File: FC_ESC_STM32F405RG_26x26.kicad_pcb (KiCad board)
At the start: 2 copper layers, 37 x 34 mm, 231 parts, among them J1 Conn_01x02, J10 Conn_01x01, J11 Conn_01x02, J12 Conn_02x02_Odd_Even, J13 ALARM, J14 LED_STRIP, J16 MOTOR, J17 MOTOR, J18 MOTOR, J19 MOTOR, J2 Conn_02x04_Odd_Even, J20 USB_A, J21 ESC_PROG, J23 ESC_PROG, J24 ESC_PROG, J25 ESC_PROG, J3 Debugger, J4 Conn_01x04, J5 RSSI, J6 Conn_01x04, J7 Conn_01x02, J8 Conn_01x04, J9 LED_STRIP, Q1 SIZ200, Q10 SIZ200, Q11 SIZ200, Q12 SIZ200, Q2 SIZ200, Q3 SIZ200, Q4 SIZ200, Q5 SIZ200, Q6 SIZ200, Q7 SIZ200, Q8 SIZ200, Q9 SIZ200, U1 EFM8BB21, U10 FD6288Q, U11 outline, U12 MPU-6000, U13 BMP280, U15 STM32F405RGTx, U16 TPS54331D, U2 EFM8BB21, U3 TPS54560BDDA, U4 FD6288Q, U5 FD6288Q, U6 AT7456, U7 EFM8BB21, U8 EFM8BB21, U9 FD6288Q, Y1 8MHz, Y2 8Mhz

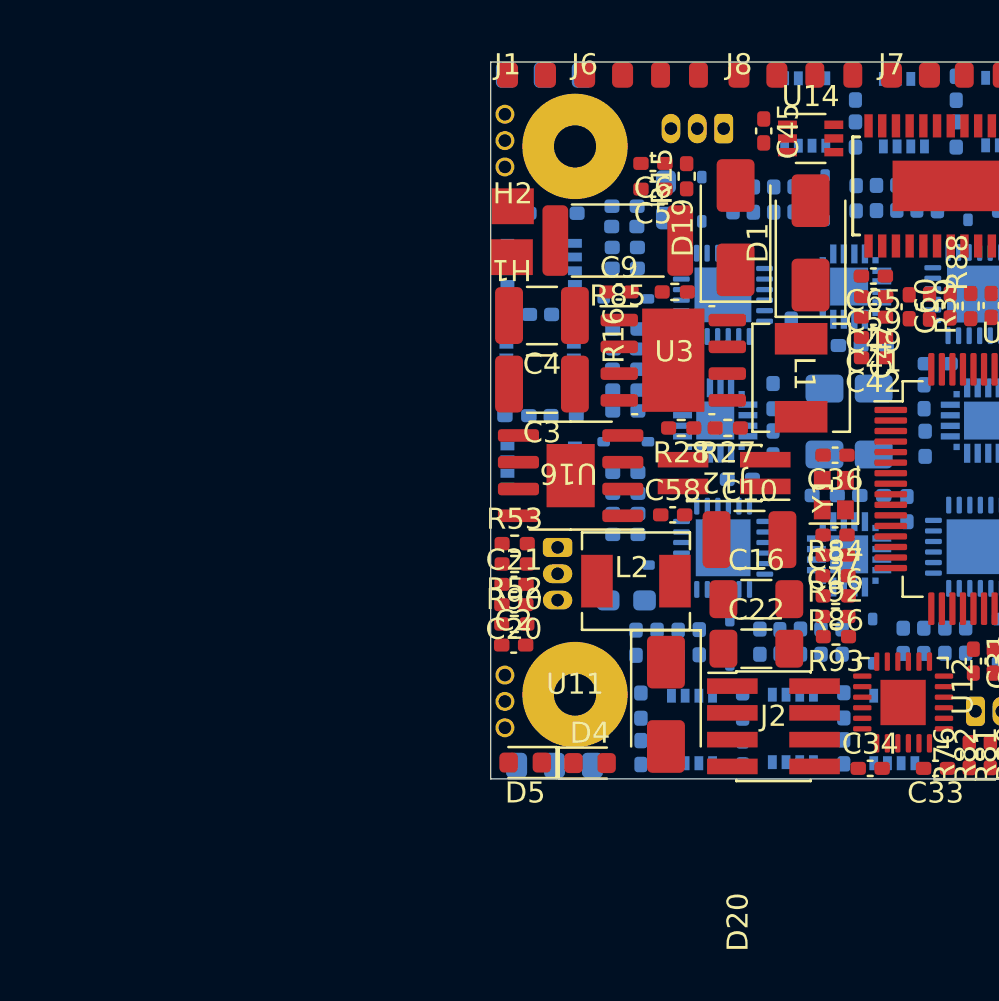
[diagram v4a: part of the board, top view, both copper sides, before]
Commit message: update placement
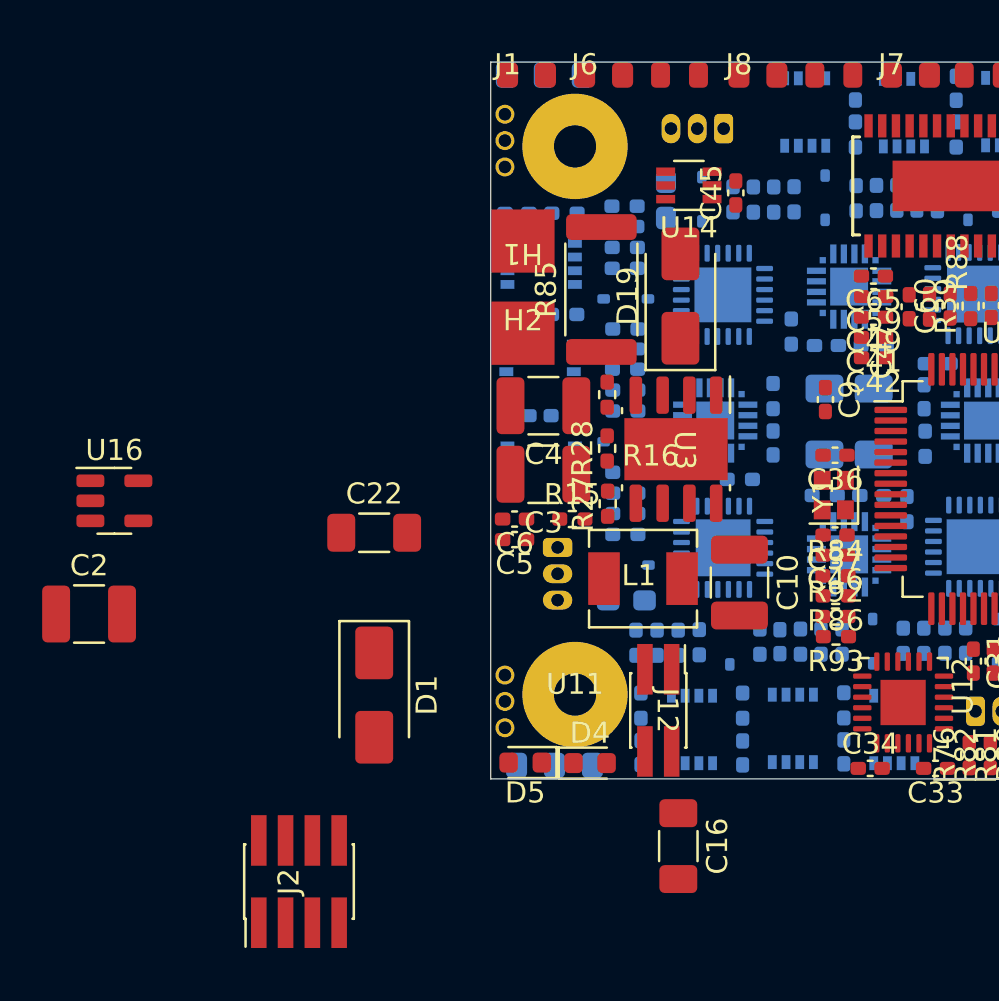
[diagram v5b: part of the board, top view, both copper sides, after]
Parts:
- removed C20: 10pF, Capacitor_SMD:C_0402_1005Metric_Pad0.74x0.62mm_HandSolder
- removed C21: 100nF, Capacitor_SMD:C_0402_1005Metric_Pad0.74x0.62mm_HandSolder
- removed C58: 8.2nF, Capacitor_SMD:C_0402_1005Metric_Pad0.74x0.62mm_HandSolder
- removed D20: SS34, Diode_SMD:D_SMA
- removed L2: 4uH, Proj_footprint:Inductor
- removed R52: 10k2, Resistor_SMD:R_0402_1005Metric_Pad0.72x0.64mm_HandSolder
- removed R53: 3.24k, Resistor_SMD:R_0402_1005Metric_Pad0.72x0.64mm_HandSolder
- removed R90: 28.7k, Resistor_SMD:R_0402_1005Metric_Pad0.72x0.64mm_HandSolder
- C2: value 1nF -> 100uF; footprint Capacitor_SMD:C_0402_1005Metric_Pad0.74x0.62mm_HandSolder -> Capacitor_SMD:C_1210_3225Metric_Pad1.33x2.70mm_HandSolder
- U16: value TPS54331D -> RT9013-33GB; footprint Proj_footprint:SOIC-8-1EP_3.9x4.9mm_P1.27mm_EP2.29x3mm -> Package_TO_SOT_SMD:SOT-23-5
- moved D1 29.8 mm to (193.0, 93.3), turned to -90 degrees
- moved J2 23.7 mm to (189.5, 102.1), turned to 90 degrees
- moved U16 21.6 mm to (180.7, 84.0), turned to 0 degrees
- moved C2 20.2 mm to (179.5, 89.4)
- moved C22 18.9 mm to (193.0, 85.6)
- moved C6 18.1 mm to (199.7, 84.9)
- moved C5 17.9 mm to (199.7, 85.9)
- moved R15 17.1 mm to (202.4, 84.9), turned to 0 degrees
- moved C16 12.3 mm to (207.5, 100.4), turned to -90 degrees
- moved L1 12.1 mm to (205.8, 87.7), turned to 0 degrees
- moved J12 11.8 mm to (206.4, 94.0), turned to -90 degrees
- moved C9 11.0 mm to (214.4, 79.2), turned to -90 degrees
- moved R27 6.74 mm to (204.1, 84.2), turned to 90 degrees
- moved U14 6.19 mm to (208.0, 69.1), turned to 180 degrees
- moved H2 6.04 mm to (200.1, 76.1)
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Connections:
- C2 pad 1: Net-(C2-Pad1) -> Net-(J2-Pin_3)
- U16 pad 1: Net-(U16-BOOT) -> +5V
- U16 pad 2: +5V -> GND
- U16 pad 4: Net-(U16-SS) -> (no net)
- U16 pad 5: Net-(U16-VSENSE) -> Net-(J2-Pin_3)

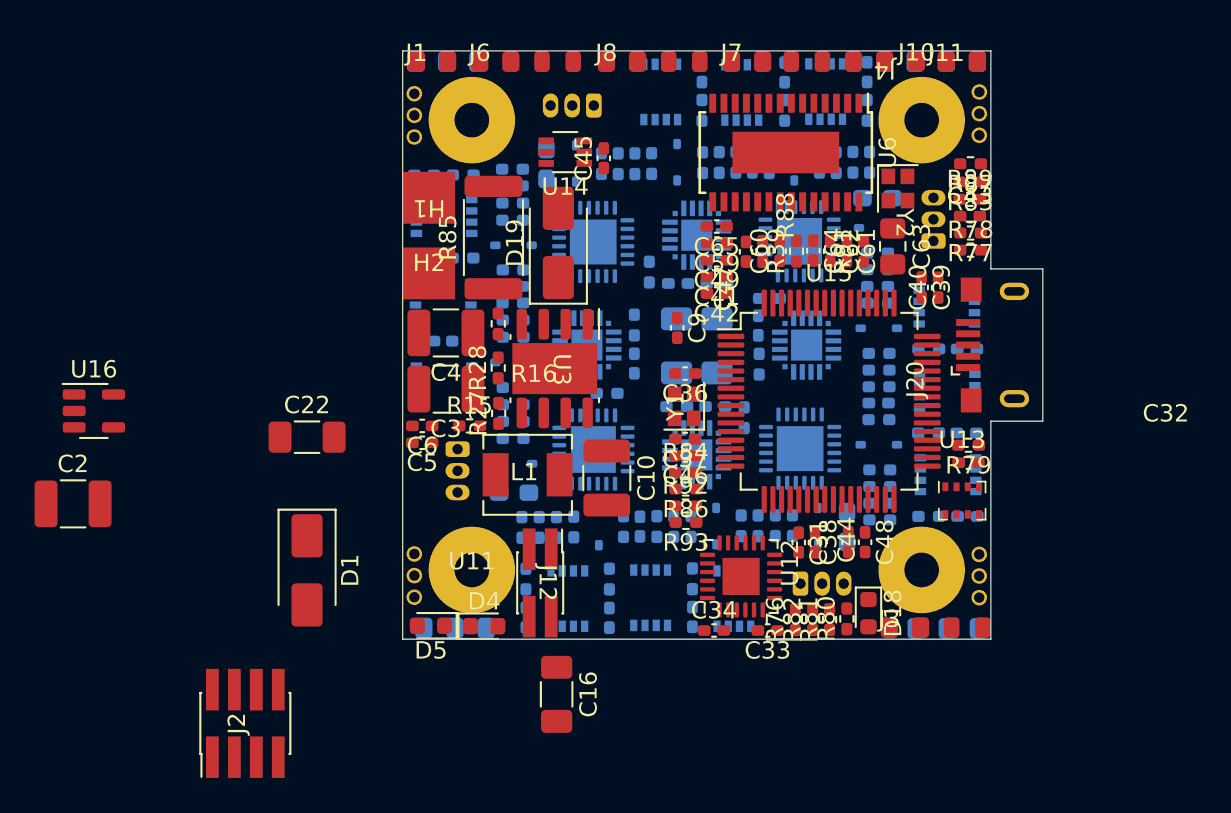
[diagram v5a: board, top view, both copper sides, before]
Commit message: update placement
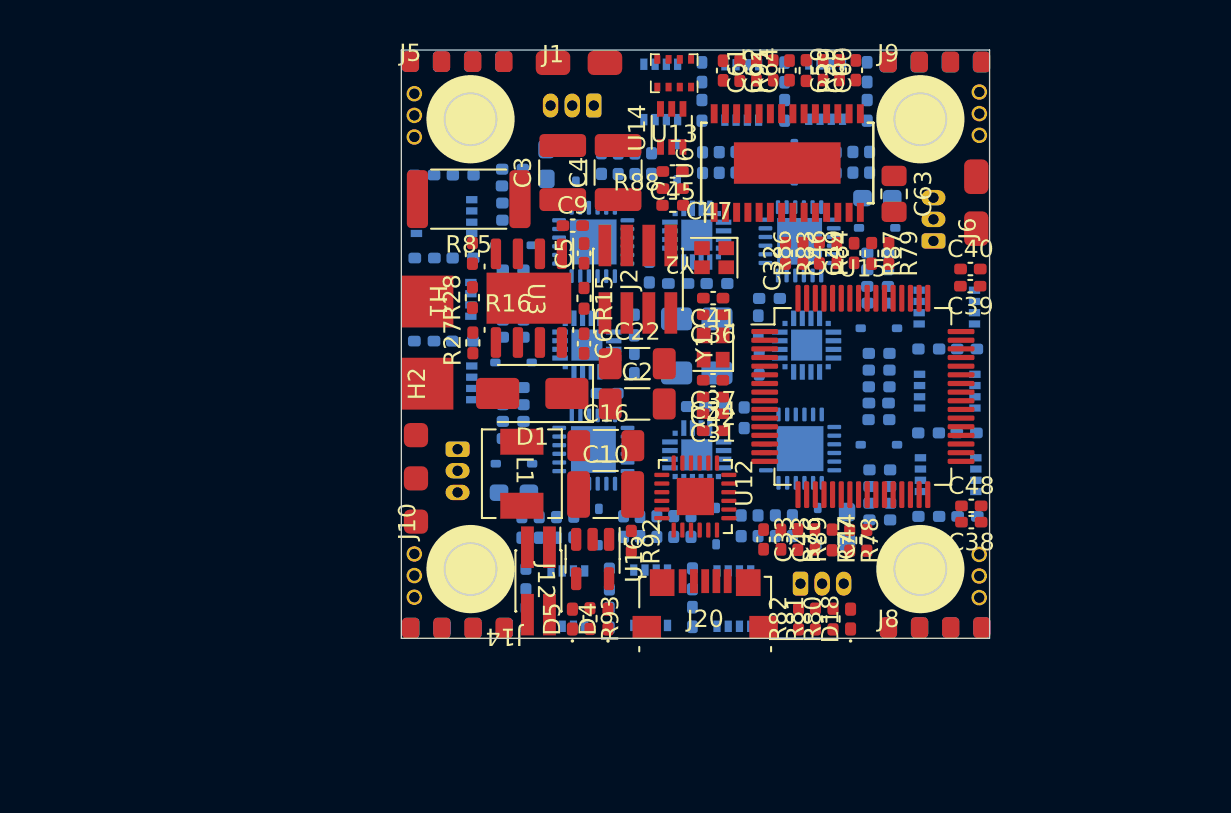
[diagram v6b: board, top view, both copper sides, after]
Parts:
- removed D19: SS34, Diode_SMD:D_SMA
- removed J11: Conn_01x02, Proj_footprint:MountingPad_1x2
- removed J13: ALARM, Proj_footprint:MountingPad_1x3
- removed J7: Conn_01x02, Proj_footprint:MountingPad_5VOUT
- added J15: Conn_01x04, Proj_footprint:MountingPad_1x4, B.Cu at (226.6, 96.6)
- added J26: Conn_01x04, Proj_footprint:MountingPad_1x4, B.Cu at (204.4, 63.8)
- C2: footprint Capacitor_SMD:C_1210_3225Metric_Pad1.33x2.70mm_HandSolder -> Capacitor_SMD:C_1206_3216Metric_Pad1.33x1.80mm_HandSolder
- D18, D4, D5: footprint LED_SMD:LED_0603_1608Metric -> LED_SMD:LED_0402_1005Metric_Pad0.77x0.64mm_HandSolder
- J1: footprint Proj_footprint:MountingPad_5VOUT -> Proj_footprint:MountingPad_1x2
- J10: value Conn_01x01 -> LED_STRIP; footprint Proj_footprint:MountingPad_1x1 -> Proj_footprint:MountingPad_1x3
- J14, J9: value LED_STRIP -> Conn_01x04; footprint Proj_footprint:MountingPad_1x3 -> Proj_footprint:MountingPad_1x4; moved to F.Cu
- J20: footprint Proj_footprint:USB_Micro-B_2P_4hole -> Proj_footprint:USB_Micro-B_SMD
- J3, J4: moved to B.Cu
- J5: value RSSI -> Conn_01x04; footprint Proj_footprint:MountingPad_1x3 -> Proj_footprint:MountingPad_1x4; moved to F.Cu
- J6: value Conn_01x04 -> Conn_01x02; footprint Proj_footprint:MountingPad_1x4 -> Proj_footprint:MountingPad_1x2
- moved J9 40.1 mm to (226.6, 63.9), turned to 0 degrees
- moved J4 39.4 mm to (204.4, 96.6)
- moved J10 39.3 mm to (199.3, 90.4), turned to 90 degrees
- moved J8 36.6 mm to (226.6, 96.6)
- moved J2 34.3 mm to (212.2, 76.4)
- moved C2 33.1 mm to (212.1, 83.6)
- moved J3 32.7 mm to (226.6, 63.9)
- moved J6 30.3 mm to (231.7, 73.5), turned to 90 degrees
- moved U16 30.1 mm to (209.5, 92.6), turned to -90 degrees
- moved U13 29.8 mm to (214.2, 64.5), turned to 180 degrees
- moved J5 29.2 mm to (199.0, 63.8)
- moved C32 26.7 mm to (217.1, 64.4), turned to -90 degrees
- moved J20 25.8 mm to (216.0, 96.6), turned to 0 degrees
- moved J14 23.8 mm to (204.4, 96.6), turned to 180 degrees
- moved R89 22.0 mm to (221.4, 91.5), turned to -90 degrees
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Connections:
- J1 pad 1: GND -> +5V
- J1 pad 2: +5V -> GND
- J10 pad 1: RCIN_INT -> +5V
- J14 pad 2: LED_STRIP -> UART1_RX
- J14 pad 3: GND -> UART1_TX
- J4 pad 1: SENS_RSSI -> +5V
- J4 pad 2: STM32_PA1 -> SENS_RSSI
- J4 pad 3: STM32_PB10 -> STM32_PA1
- J4 pad 4: STM32_PB11 -> GND
- J5 pad 1: +5V -> SPI2_CS
- J5 pad 2: RSSI_IN -> SPI2_MOSI
- J5 pad 3: GND -> SPI2_MISO
- J6 pad 1: SPI2_CS -> +5V
- J6 pad 2: SPI2_MOSI -> GND
- J8 pad 1: UART6_TX -> +5V
- J8 pad 2: UART6_RX -> UART6_TX
- J8 pad 3: UART1_RX -> UART6_RX
- J8 pad 4: UART1_TX -> GND
- J9 pad 2: PWM_OUT -> OSD_VIDEO_OUT
- J9 pad 3: GND -> OSD_VIDEO_IN
- U15 pad 39: PWM_OUT -> unconnected-(U15-PC8-Pad39)
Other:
- board size 37 x 34 mm -> 34 x 34 mm

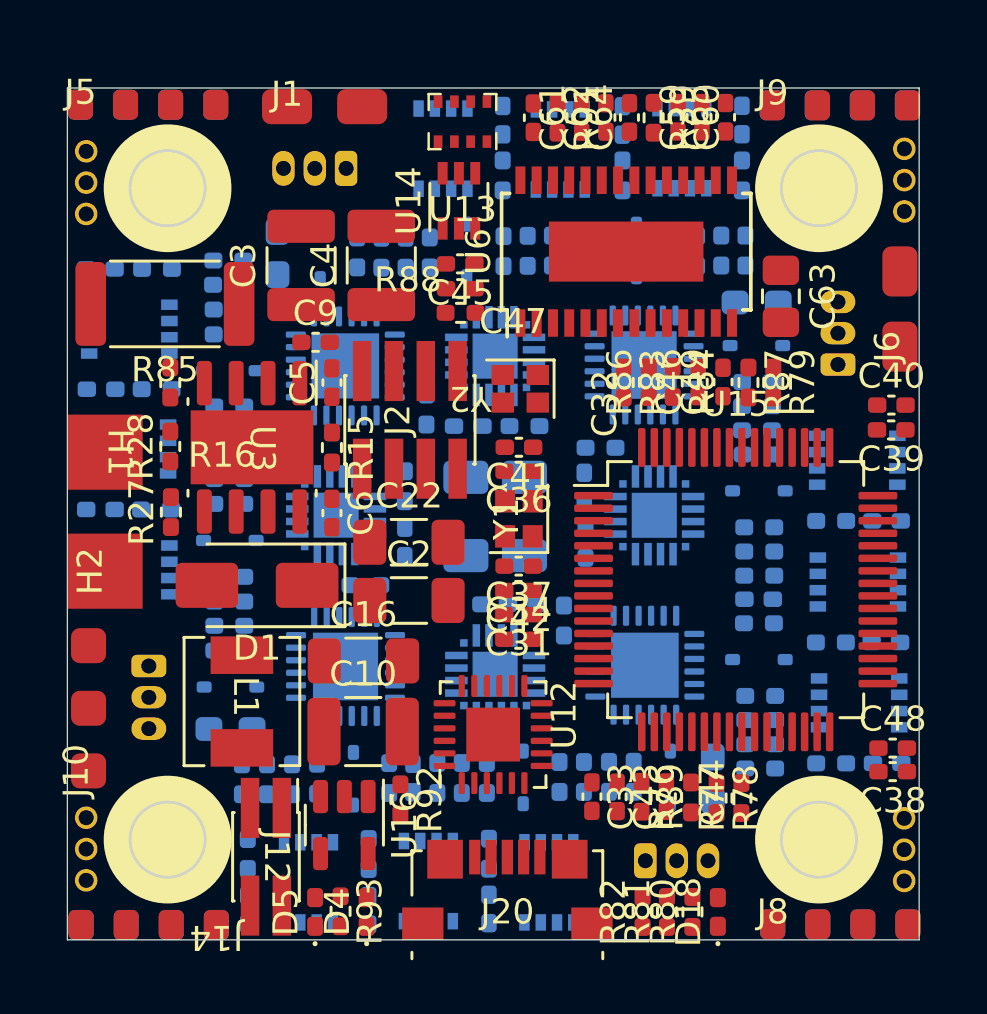
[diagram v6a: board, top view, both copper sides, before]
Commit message: update placement
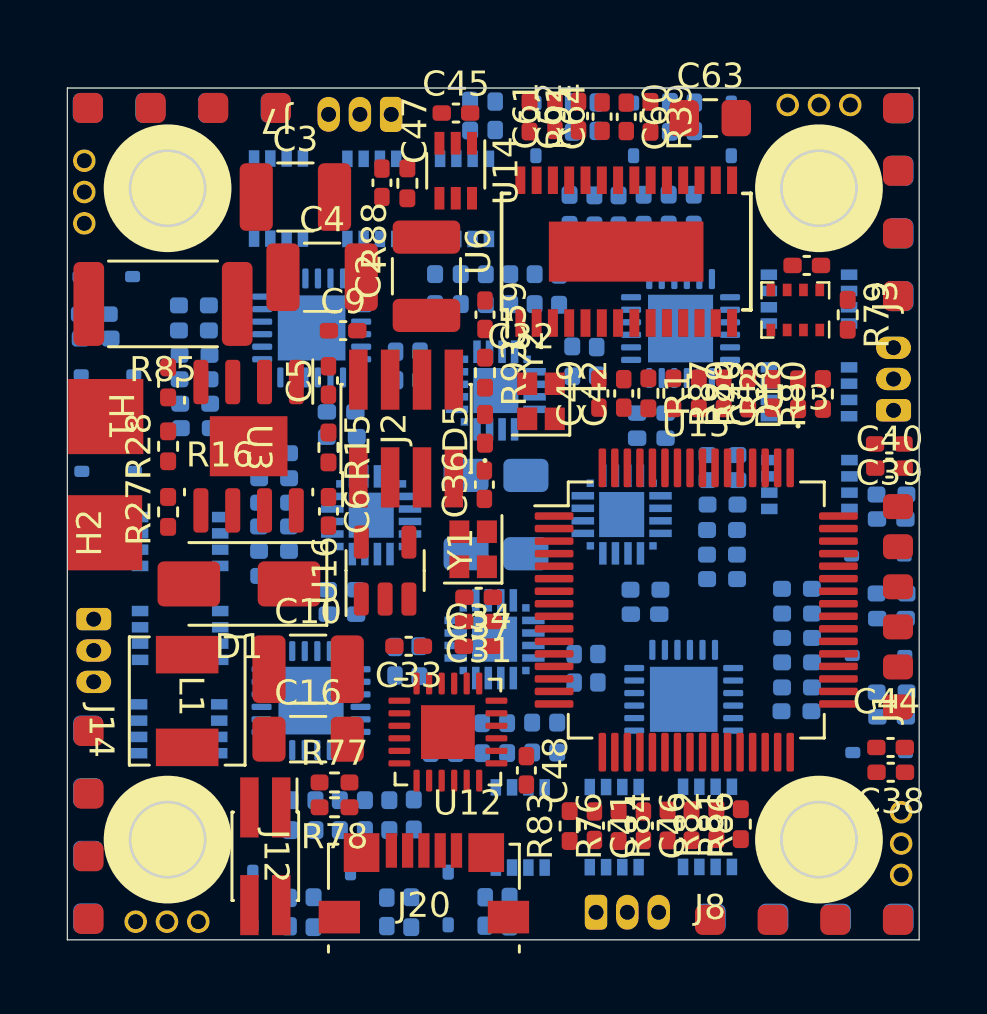
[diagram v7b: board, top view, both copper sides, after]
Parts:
- removed C22: 100uF, Capacitor_SMD:C_1206_3216Metric_Pad1.33x1.80mm_HandSolder
- removed C65: 100nF, Capacitor_SMD:C_0402_1005Metric_Pad0.74x0.62mm_HandSolder
- removed D4: LED_RED, LED_SMD:LED_0402_1005Metric_Pad0.77x0.64mm_HandSolder
- removed J10: LED_STRIP, Proj_footprint:MountingPad_1x3
- removed J5: Conn_01x04, Proj_footprint:MountingPad_1x4
- removed J6: Conn_01x02, Proj_footprint:MountingPad_1x2
- removed R41: 1k, Resistor_SMD:R_0402_1005Metric_Pad0.72x0.64mm_HandSolder
- removed R92: 100R, Resistor_SMD:R_0402_1005Metric_Pad0.72x0.64mm_HandSolder
- added J7: Conn_01x04, Proj_footprint:MountingPad_1x4, F.Cu at (206.8, 64.0)
- C2: footprint Capacitor_SMD:C_1206_3216Metric_Pad1.33x1.80mm_HandSolder -> Capacitor_SMD:C_1210_3225Metric_Pad1.33x2.70mm_HandSolder
- C50, C51, C52, C53: footprint Capacitor_SMD:C_0603_1608Metric_Pad1.08x0.95mm_HandSolder -> Capacitor_SMD:C_0402_1005Metric_Pad0.74x0.62mm_HandSolder
- J1: value Conn_01x02 -> Conn_01x06; footprint Proj_footprint:MountingPad_1x2 -> Proj_footprint:MountingPad_1x6
- J3: moved to F.Cu
- J9: moved to B.Cu
- R1, R2, R40: value 1k -> 2k2; moved to F.Cu
- moved J1 34.2 mm to (231.6, 87.9), turned to 90 degrees
- moved R93 22.3 mm to (215.1, 74.5)
- moved R30 21.7 mm to (218.5, 68.0), turned to 90 degrees
- moved R67 21.5 mm to (227.6, 83.2), turned to 0 degrees
- moved R32 21.5 mm to (212.3, 92.2), turned to -90 degrees
- moved R80 21.3 mm to (228.6, 75.4)
- moved R69 21.2 mm to (203.6, 76.8), turned to 180 degrees
- moved D18 20.9 mm to (227.6, 75.4)
- moved D5 20.4 mm to (215.1, 76.8)
- moved R29 20.0 mm to (221.5, 68.0), turned to 90 degrees
- moved R66 19.7 mm to (227.6, 86.1), turned to 0 degrees
- moved R31 19.7 mm to (209.4, 92.2), turned to -90 degrees
- moved R68 19.5 mm to (203.6, 73.8), turned to 180 degrees
- moved C46 17.8 mm to (221.5, 92.6), turned to -90 degrees
- moved R83 17.8 mm to (218.5, 92.6), turned to 90 degrees
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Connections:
- net LED_PWR_5V renamed Net-(J12-Pin_3)
- C2 pad 1: Net-(J2-Pin_3) -> LED_PWR_3V3
- J1 pad 2: GND -> SPI2_CS
- R1 pad 1: ESC1_RX -> 3V3_FC
- R1 pad 2: Net-(U1-P0.0) -> BOOT0
- R2 pad 1: ESC3_RX -> GND
- R2 pad 2: Net-(U2-P0.0) -> BOOT1
- R40 pad 1: ESC2_RX -> 3V3_FC
- R40 pad 2: Net-(U7-P0.0) -> BOOT1
- R87 pad 2: 3V3_FC -> BOOT0
- U1 pad 2: Net-(U1-P0.0) -> ESC1_RX
- U15 pad 28: unconnected-(U15-PB2-Pad28) -> BOOT1
- U15 pad 60: 3V3_FC -> BOOT0
- U2 pad 2: Net-(U2-P0.0) -> ESC3_RX
- U7 pad 2: Net-(U7-P0.0) -> ESC2_RX
- U8 pad 2: Net-(U8-P0.0) -> ESC4_RX
- Y2 pad 1: Net-(U6-CLKIN) -> Net-(U6-XFB)
- Y2 pad 2: Net-(U6-XFB) -> Net-(U6-CLKIN)
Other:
- copper layers 2 -> 4

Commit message: update routing
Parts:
- moved R43 1.68 mm to (227.6, 89.7)
- moved R4 1.62 mm to (225.1, 68.0)
- moved R7 1.30 mm to (206.1, 92.1)
- moved R46 1.25 mm to (203.6, 70.6)
- moved C54 1.17 mm to (210.6, 76.2)
- moved R6 1.15 mm to (210.6, 77.2)
- moved R59 0.98 mm to (203.5, 76.8)
- moved R47 0.98 mm to (203.5, 75.8)
- moved R17 0.97 mm to (223.4, 68.0)
- moved R69 0.97 mm to (203.5, 77.7)
- moved C57 0.96 mm to (219.6, 75.1), turned to -90 degrees
- moved R45 0.93 mm to (218.6, 75.0)
- moved R20 0.91 mm to (212.2, 92.2)
- moved R8 0.91 mm to (211.3, 92.2)
- moved R32 0.91 mm to (213.2, 92.2)
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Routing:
- net 3V3_ESC: track 0.00 -> 10.8 mm
- net +5V: track 0.00 -> 10.4 mm
- net ESC4_VB2: track 0.00 -> 7.33 mm, vias 0 -> 2
- net ESC4_VB3: track 0.00 -> 6.16 mm, vias 0 -> 2
- net ESC4_LO3: track 0.00 -> 6.00 mm
- net ESC1_LO3: track 0.00 -> 6.00 mm
- net ESC3_VB2: track 0.00 -> 5.94 mm, vias 0 -> 2
- net ESC1_Acom: track 0.00 -> 5.86 mm, vias 0 -> 2
- net ESC3_LO3: track 0.00 -> 5.84 mm
- net ESC2_LO3: track 0.00 -> 5.71 mm
- net ESC1_VB3: track 0.00 -> 5.59 mm, vias 0 -> 2
- net ESC4_MC: track 0.00 -> 5.59 mm, vias 0 -> 1
- net ESC4_VB1: track 0.00 -> 5.49 mm, vias 0 -> 1
- net ESC1_VS2: track 0.00 -> 5.46 mm, vias 0 -> 2
- net ESC4_MA: track 0.00 -> 5.36 mm, vias 0 -> 1
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- added copper zone on B.Cu, net ESC1_VS1
- added copper zone on B.Cu, net ESC1_VS2
- added copper zone on B.Cu, net ESC1_VS3
- added copper zone on B.Cu, net ESC2_VS1
- added copper zone on B.Cu, net ESC2_VS2
- added copper zone on B.Cu, net ESC2_VS3
- added copper zone on B.Cu, net ESC3_VS1
- added copper zone on B.Cu, net ESC3_VS2
- added copper zone on B.Cu, net ESC3_VS3
- added copper zone on B.Cu, net ESC4_VS1
- added copper zone on B.Cu, net ESC4_VS2
- added copper zone on B.Cu, net ESC4_VS3
- added copper zone on B.Cu, net GND
- added copper zone on F.Cu, net GND
- added copper zone on F.Cu, net Net-(D1-K)
- added copper zone on F.Cu, net Net-(J12-Pin_3)
- added copper zone on F.Cu, net Net-(U14-+)
- added copper zone on F.Cu, net V_BAT
